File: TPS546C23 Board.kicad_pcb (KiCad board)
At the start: 2 copper layers, 59.9 x 54.9 mm, 40 parts, among them IC1 TPS546C23RVFT, J1 Conn_01x01, J2 Conn_01x01, J3 Conn_01x01, J4 Conn_01x01, J7 Conn_01x02_Pin

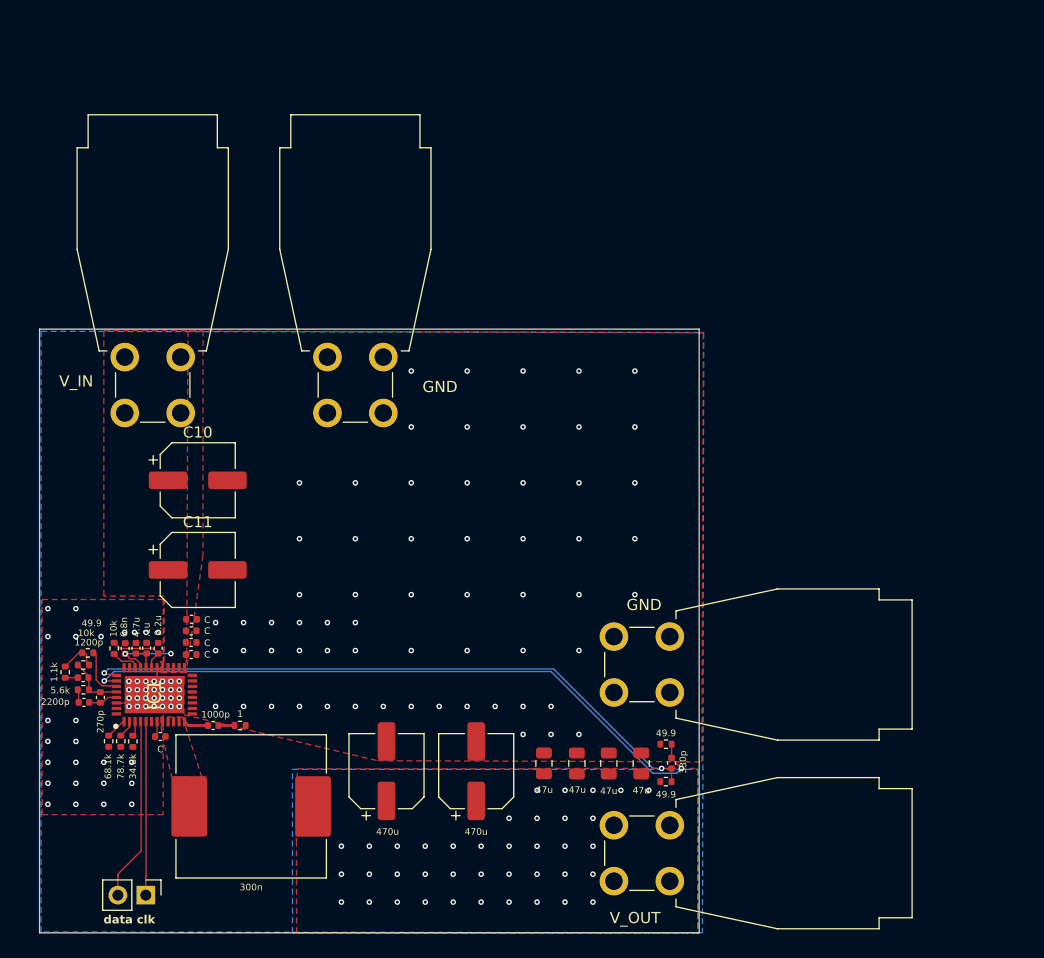
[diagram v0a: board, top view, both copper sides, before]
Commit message: added Rbias for full voltage range
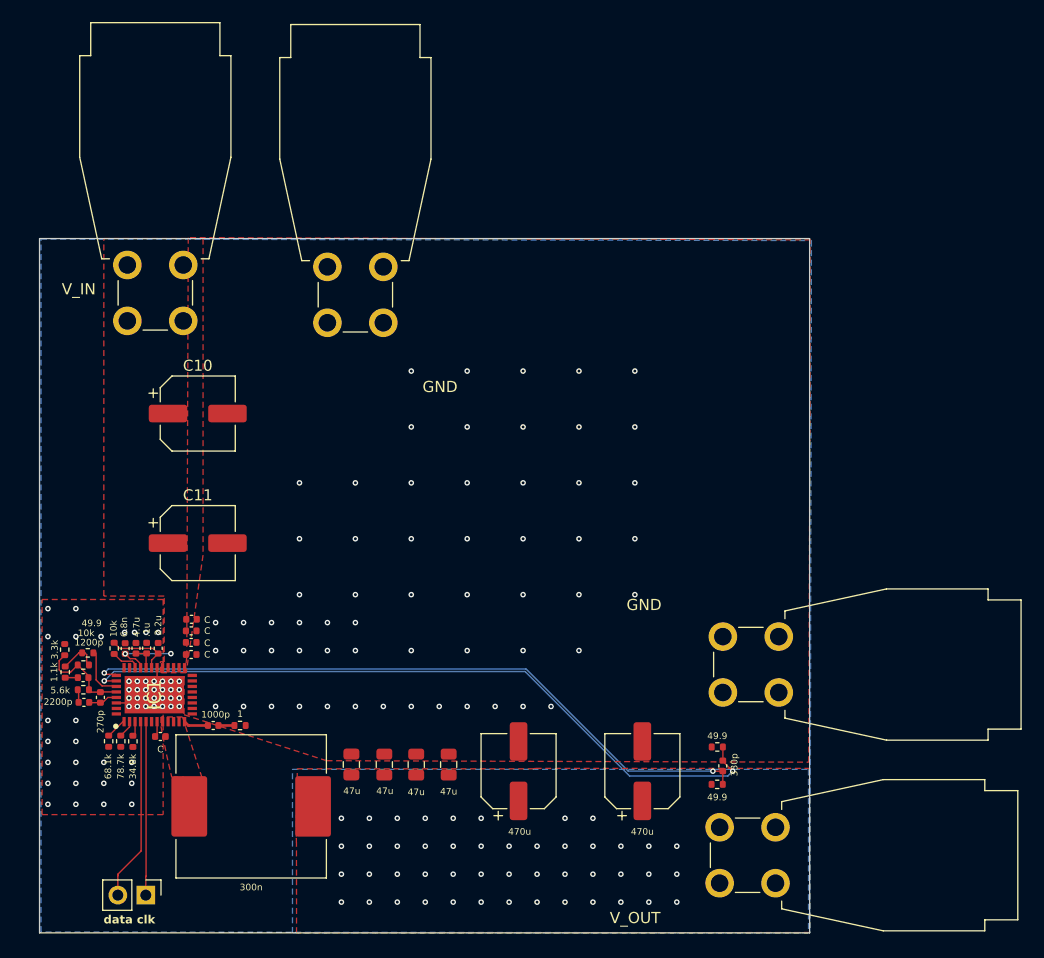
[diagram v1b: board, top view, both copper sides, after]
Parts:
- added Rbias1: 3.3k, Resistor_SMD:R_0402_1005Metric, F.Cu at (197.1, 66.0)
- moved C4 17.5 mm to (223.2, 76.4)
- moved C5 17.5 mm to (226.2, 76.4)
- moved C6 17.5 mm to (229.1, 76.4)
- moved C9 17.5 mm to (232.0, 76.4)
- moved C8 15.1 mm to (249.6, 77.0)
- moved C7 12.0 mm to (238.3, 77.0)
- moved J3 9.90 mm to (262.0, 69.8)
- moved J4 9.61 mm to (261.7, 87.2)
- moved J1 8.37 mm to (207.9, 31.0)
- moved J2 8.20 mm to (226.1, 31.2)
- moved C10 6.06 mm to (209.2, 44.5)
- moved Crsn1 4.67 mm to (256.9, 76.5)
- moved Rsn1 4.67 mm to (256.4, 74.8)
- moved Rsp1 4.67 mm to (256.4, 78.2)
- moved C11 2.44 mm to (209.2, 56.3)
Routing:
- net rsp: track 57.8 -> 62.6 mm
- net rsn: track 60.5 -> 65.3 mm
- net Net-(IC1-FB): track 5.26 -> 8.85 mm
- net V_A: vias 39 -> 47
- net AGND: vias 116 -> 113
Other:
- board size 59.9 x 54.9 mm -> 70 x 63.1 mm

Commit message: added voltage divider resistor, changed to 4 layer
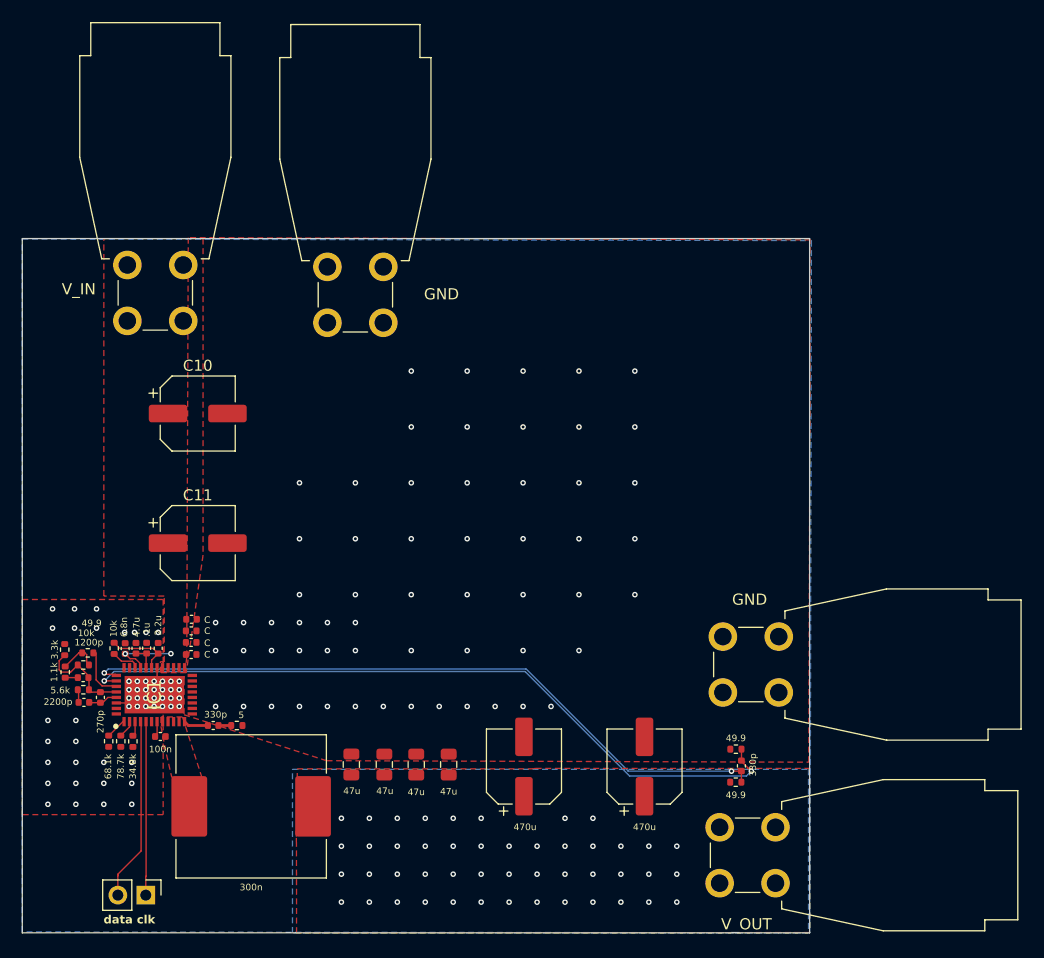
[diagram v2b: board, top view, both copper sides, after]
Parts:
- CL1: value 1000p -> 330p
- C_boot1: value C -> 100n
- RL1: value 1 -> 5
- moved Rsn1 1.70 mm to (258.1, 75.0)
- moved Rsp1 1.70 mm to (258.1, 78.0)
- moved Crsn1 1.69 mm to (258.6, 76.5)
- moved C7 0.65 mm to (238.8, 76.6)
- moved C8 0.46 mm to (249.8, 76.6)
- moved RL1 0.29 mm to (212.8, 72.8)
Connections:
- net rsn renamed rs-
- net rsp renamed rs+
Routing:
- net rs+: track 62.6 -> 64.3 mm
- net rs-: track 65.3 -> 67.0 mm
- net AGND: vias 113 -> 114
- added copper zone on In1.Cu, net AGND
- added copper zone on In2.Cu, net AGND
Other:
- board size 70 x 63.1 mm -> 71.6 x 63.1 mm
- copper layers 2 -> 4
